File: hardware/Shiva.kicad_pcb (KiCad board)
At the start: 2 copper layers, 99.8 x 99.8 mm, 109 parts, among them J1 JACK_FEMALE_STEREO, J2 JACK_FEMALE_STEREO, J3 JACK_FEMALE_STEREO, J4 JACK_FEMALE_STEREO, J5 JACK_FEMALE_STEREO, J6 JACK_FEMALE_STEREO, J7 JACK_FEMALE_STEREO, J8 JACK_FEMALE_STEREO, P1 DIN_5, Q1 2N7002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

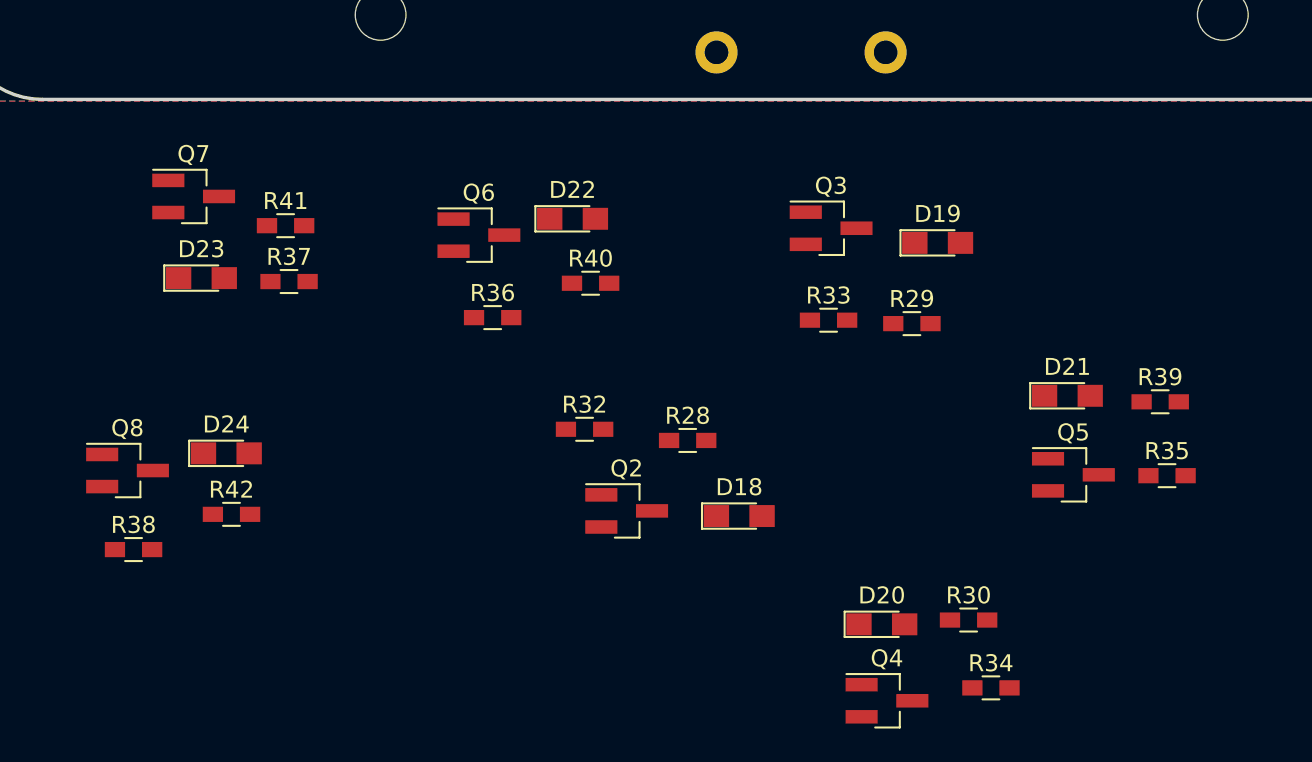
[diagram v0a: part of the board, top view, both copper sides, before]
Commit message: Reload footprints
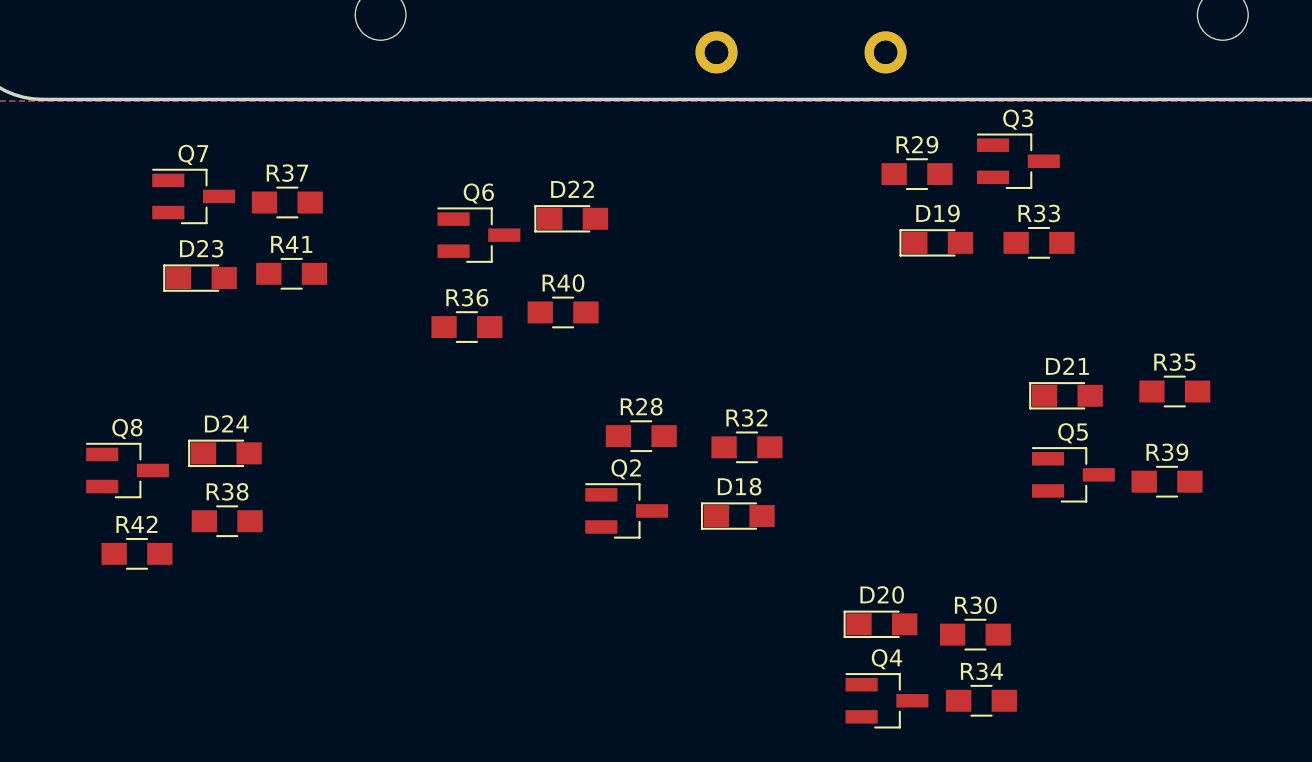
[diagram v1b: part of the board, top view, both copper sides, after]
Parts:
- R28, R29, R30, R32, R33, R34, R35, R36, R37, R38, R39, R40, R41, R42: footprint Resistors_SMD:R_0603_HandSoldering -> Resistors_SMD:R_0805_HandSoldering
- moved R33 13.3 mm to (158.3, 161.0)
- moved Q3 11.8 mm to (157.1, 156.2)
- moved R32 9.66 mm to (141.1, 173.1)
- moved R29 8.84 mm to (151.1, 157.0)
- moved R42 6.06 mm to (105.0, 179.4)
- moved R38 5.79 mm to (110.3, 177.5)
- moved R35 5.00 mm to (166.4, 169.8)
- moved R39 4.74 mm to (165.9, 175.2)
- moved R37 4.67 mm to (113.9, 158.6)
- moved R41 2.87 mm to (114.1, 162.9)
- moved R28 2.75 mm to (134.8, 172.5)
- moved R40 2.37 mm to (130.2, 165.2)
- moved R36 1.62 mm to (124.5, 166.0)
- moved R30 0.95 mm to (154.6, 184.2)
- moved R34 0.94 mm to (154.9, 188.1)

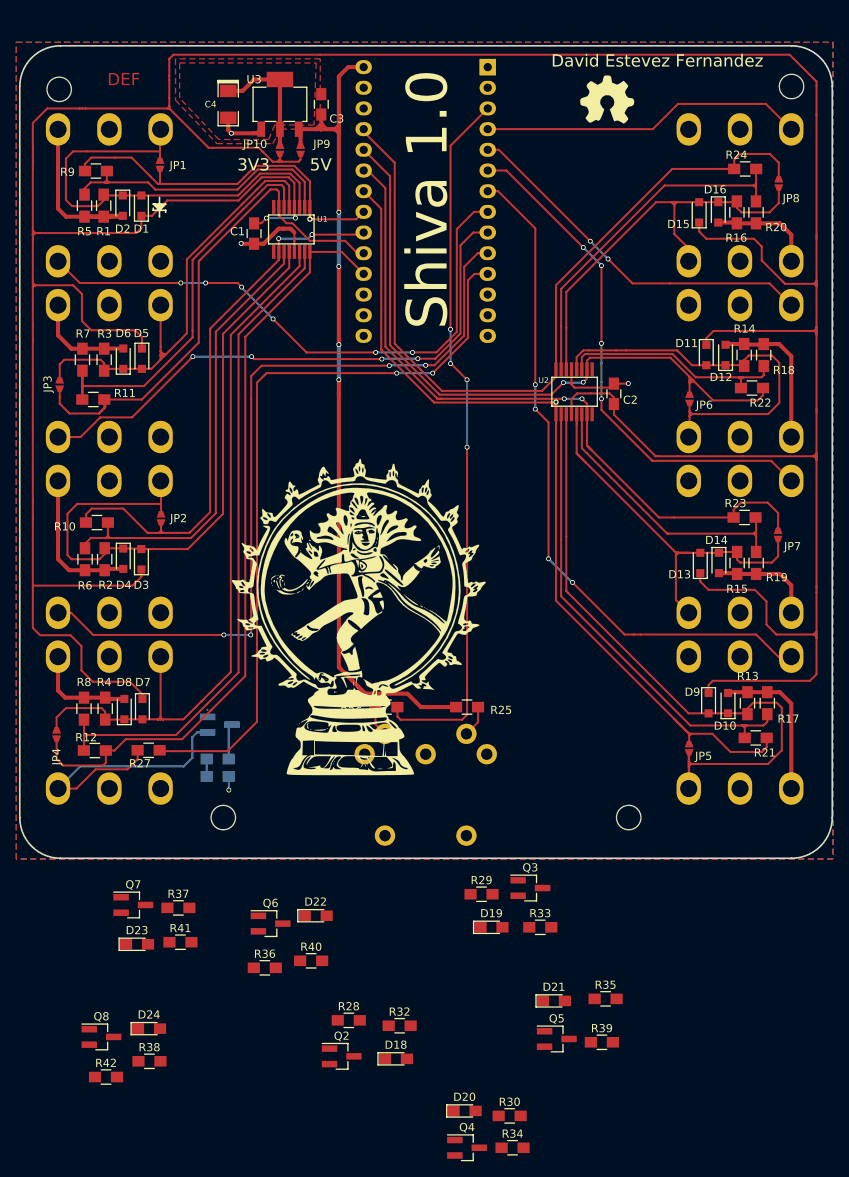
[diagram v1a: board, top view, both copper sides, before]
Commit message: Add KEDs for channels 2-8
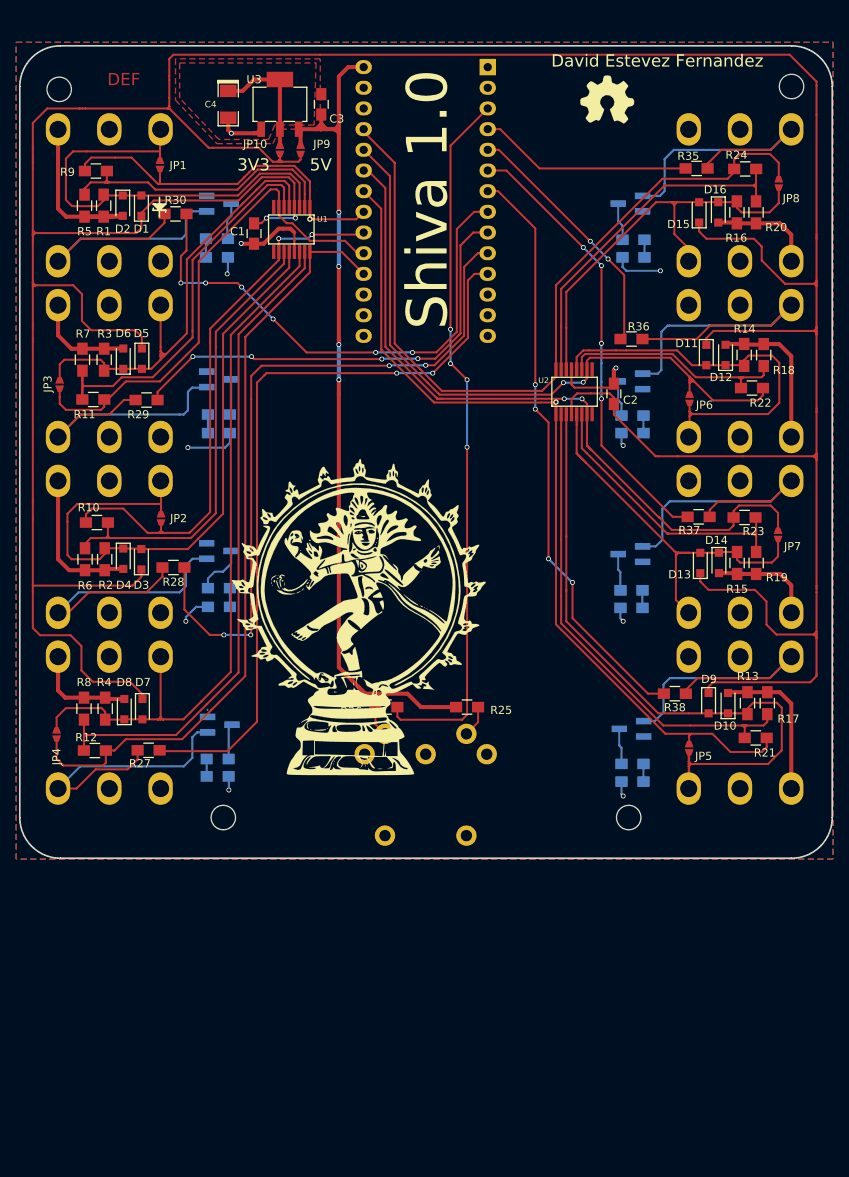
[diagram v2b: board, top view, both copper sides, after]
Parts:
- D18, D19, D20, D21, D22, D23, D24, Q2, Q3, Q4, Q5, Q6, Q7, Q8, R32, R33, R34, R39, R40, R41, R42: moved to B.Cu
- moved Q4 119.9 mm to (118.9, 72.1)
- moved R30 118.2 mm to (113.5, 73.4)
- moved R34 117.4 mm to (118.6, 76.5)
- moved D20 109.2 mm to (118.6, 78.7)
- moved Q5 103.0 mm to (169.4, 72.1), turned to 180 degrees
- moved R35 102.6 mm to (177.5, 67.8), turned to 180 degrees
- moved R39 98.7 mm to (169.8, 76.6), turned to 180 degrees
- moved D21 91.9 mm to (169.8, 78.7), turned to 180 degrees
- moved R36 89.4 mm to (169.5, 88.8), turned to 180 degrees
- moved R37 79.9 mm to (177.8, 110.6), turned to 180 degrees
- moved Q6 79.9 mm to (169.4, 94.0), turned to 180 degrees
- moved R38 78.8 mm to (174.9, 132.3), turned to 180 degrees
- moved R40 77.7 mm to (169.7, 98.2), turned to 180 degrees
- moved Q8 75.3 mm to (169.5, 136.7), turned to 180 degrees
- moved R42 75.2 mm to (169.7, 141.0), turned to 180 degrees
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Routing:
- net /CHANNEL_06_SW: track 5.53 -> 46.4 mm
- net /CHANNEL_08_SW: track 2.75 -> 39.7 mm
- net /CHANNEL_04_SW: track 6.86 -> 41.2 mm
- net /CHANNEL_05_SW: track 5.57 -> 37.7 mm
- net VCC: track 474.2 -> 498.1 mm, vias 3 -> 10
- net /DETECT_07: track 35.2 -> 55.1 mm, vias 3 -> 4
- net /CHANNEL_02_SW: track 23.6 -> 40.4 mm, vias 1 -> 0
- net /DETECT_03: track 41.5 -> 56.3 mm, vias 2 -> 4
- net /DETECT_02: track 75.4 -> 86.7 mm, vias 3 -> 4
- net /DETECT_06: track 41.4 -> 31.2 mm
- net /DETECT_08: track 82.2 -> 72.6 mm
- net /DETECT_05: track 35.4 -> 26.3 mm
- net /CHANNEL_07_SW: track 30.4 -> 38.3 mm, vias 1 -> 0
- net Net-(Q2-Pad3): track 0.00 -> 6.35 mm
- net /CHANNEL_03_SW: track 29.3 -> 34.5 mm, vias 2 -> 0
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
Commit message: Fix some tracks to make them much more better
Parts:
- moved G*** 21.3 mm to (144.5, 128.2)
- moved G*** 12.0 mm to (145.7, 115.8)
- moved G*** 1.58 mm to (142.7, 124.8)
- moved C3 0.94 mm to (132.4, 59.9)
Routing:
- net /CHANNEL_06_SW: track 46.4 -> 28.2 mm, vias 0 -> 1
- net /CHANNEL_08_SW: track 39.7 -> 24.0 mm, vias 0 -> 1
- net /CHANNEL_02_SW: track 40.4 -> 24.7 mm, vias 0 -> 1
- net /CHANNEL_04_SW: track 41.2 -> 26.3 mm, vias 0 -> 1
- net /CHANNEL_05_SW: track 37.7 -> 24.5 mm, vias 0 -> 1
- net VCC: track 498.1 -> 509.5 mm
- net /CHANNEL_07_SW: track 38.3 -> 27.3 mm, vias 0 -> 1
- net /CHANNEL_01_SW: track 37.1 -> 26.5 mm, vias 0 -> 1
- net /CHANNEL_03_SW: track 34.5 -> 26.3 mm, vias 0 -> 1
- net GND: track 160.2 -> 164.8 mm
- net +5V: track 105.4 -> 106.7 mm
- net /CHANNEL_05: track 99.8 -> 100.8 mm
- net /CHANNEL_07: track 90.9 -> 90.3 mm
- net Net-(D5-Pad2): track 58.3 -> 58.8 mm

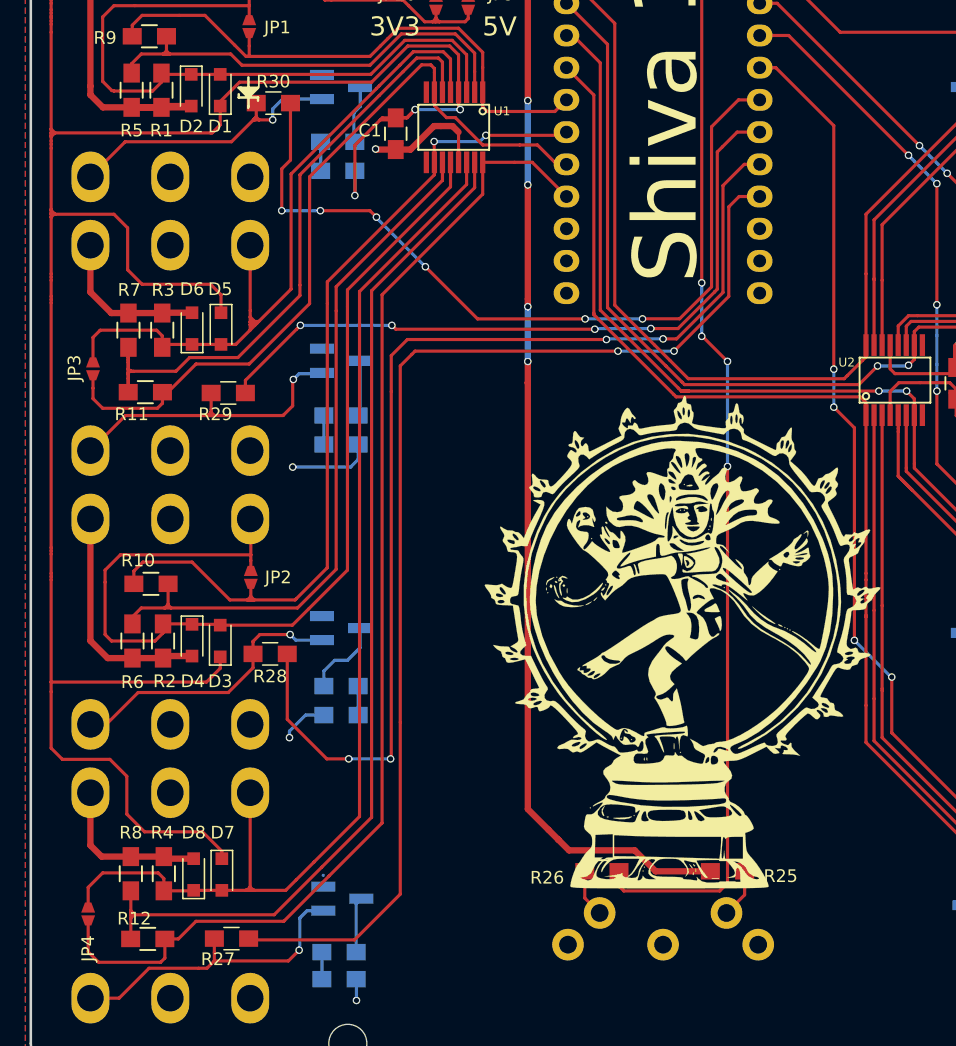
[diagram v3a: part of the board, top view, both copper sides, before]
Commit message: Add 5-way joystick as user interface
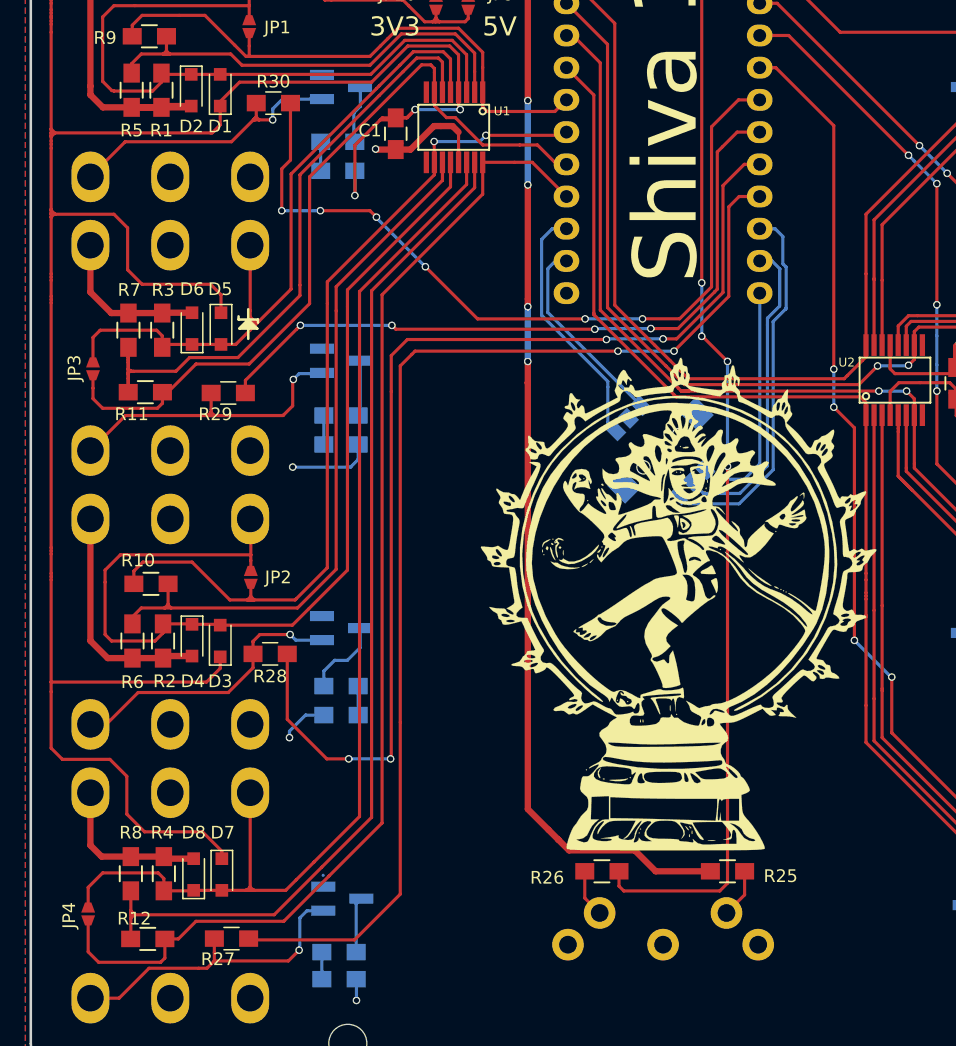
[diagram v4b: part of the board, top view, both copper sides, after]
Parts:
- removed the G*** at (142.7, 124.8)
- added SW1: PASSIVES_JOYSTICK_5_WAY, def-footprints:Switches_ALPS-SKRHAAE010, B.Cu at (144.1, 100.8)
- moved G*** 7.42 mm to (144.3, 120.8)
- moved G*** 3.01 mm to (145.4, 112.8)
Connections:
- BOARD1 pad 12: Net-(BOARD1-Pad12) -> /JOY_C
- BOARD1 pad 13: Net-(BOARD1-Pad13) -> /JOY_PRESS
- BOARD1 pad 14: Net-(BOARD1-Pad14) -> /JOY_A
- BOARD1 pad 16: Net-(BOARD1-Pad16) -> /JOY_B
- BOARD1 pad 17: Net-(BOARD1-Pad17) -> /JOY_D
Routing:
- net /JOY_C: track 0.00 -> 29.8 mm
- net /JOY_PRESS: track 0.00 -> 25.0 mm
- net /JOY_D: track 0.00 -> 19.8 mm
- net /JOY_A: track 0.00 -> 18.6 mm
- net /JOY_B: track 0.00 -> 15.6 mm

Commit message: Add last minute fixes
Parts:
- moved C3 0.91 mm to (133.3, 59.9)
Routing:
- net GND: track 164.8 -> 163.9 mm
- net +5V: track 106.7 -> 107.7 mm
- net VCC: track 509.5 -> 510.2 mm
- net /CHANNEL_04: track 46.7 -> 47.4 mm
- net Net-(D1-Pad2): track 55.8 -> 56.4 mm
